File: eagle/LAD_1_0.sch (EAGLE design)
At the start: 14 parts, among them X1 A0, X10 A, X2 A1, X3 A2, X4 A3, X5 A, X6 A0, X7 A1, X8 A2, X9 A3

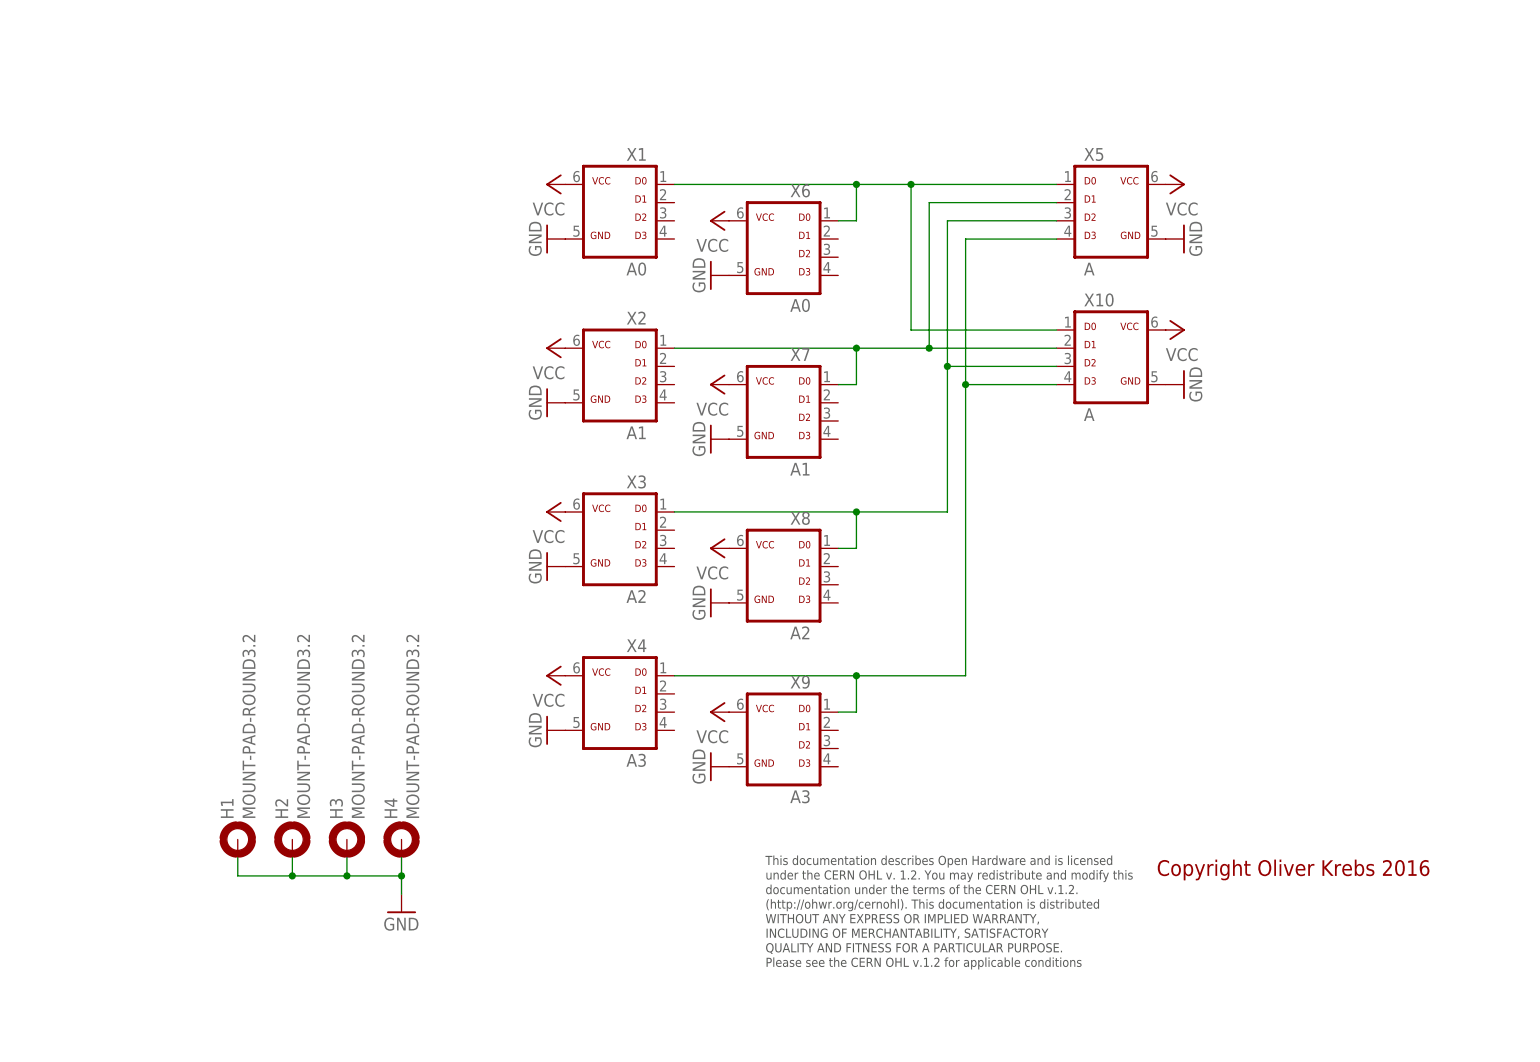
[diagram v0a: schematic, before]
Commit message: Add new tetra-Board and arduino files
Add AMP_1_0, AVC_1_0, D18_1_1, IOP_1_2, MIC_1_0, PIN_1_1, POT_1_0, PWA_1_0, PWR_1_0, RGF 2.0, SOC_2_0, VLT_1_0
Add mex_nano_shield_keyboard, mex_nano_shied_numbers

New arduino projects
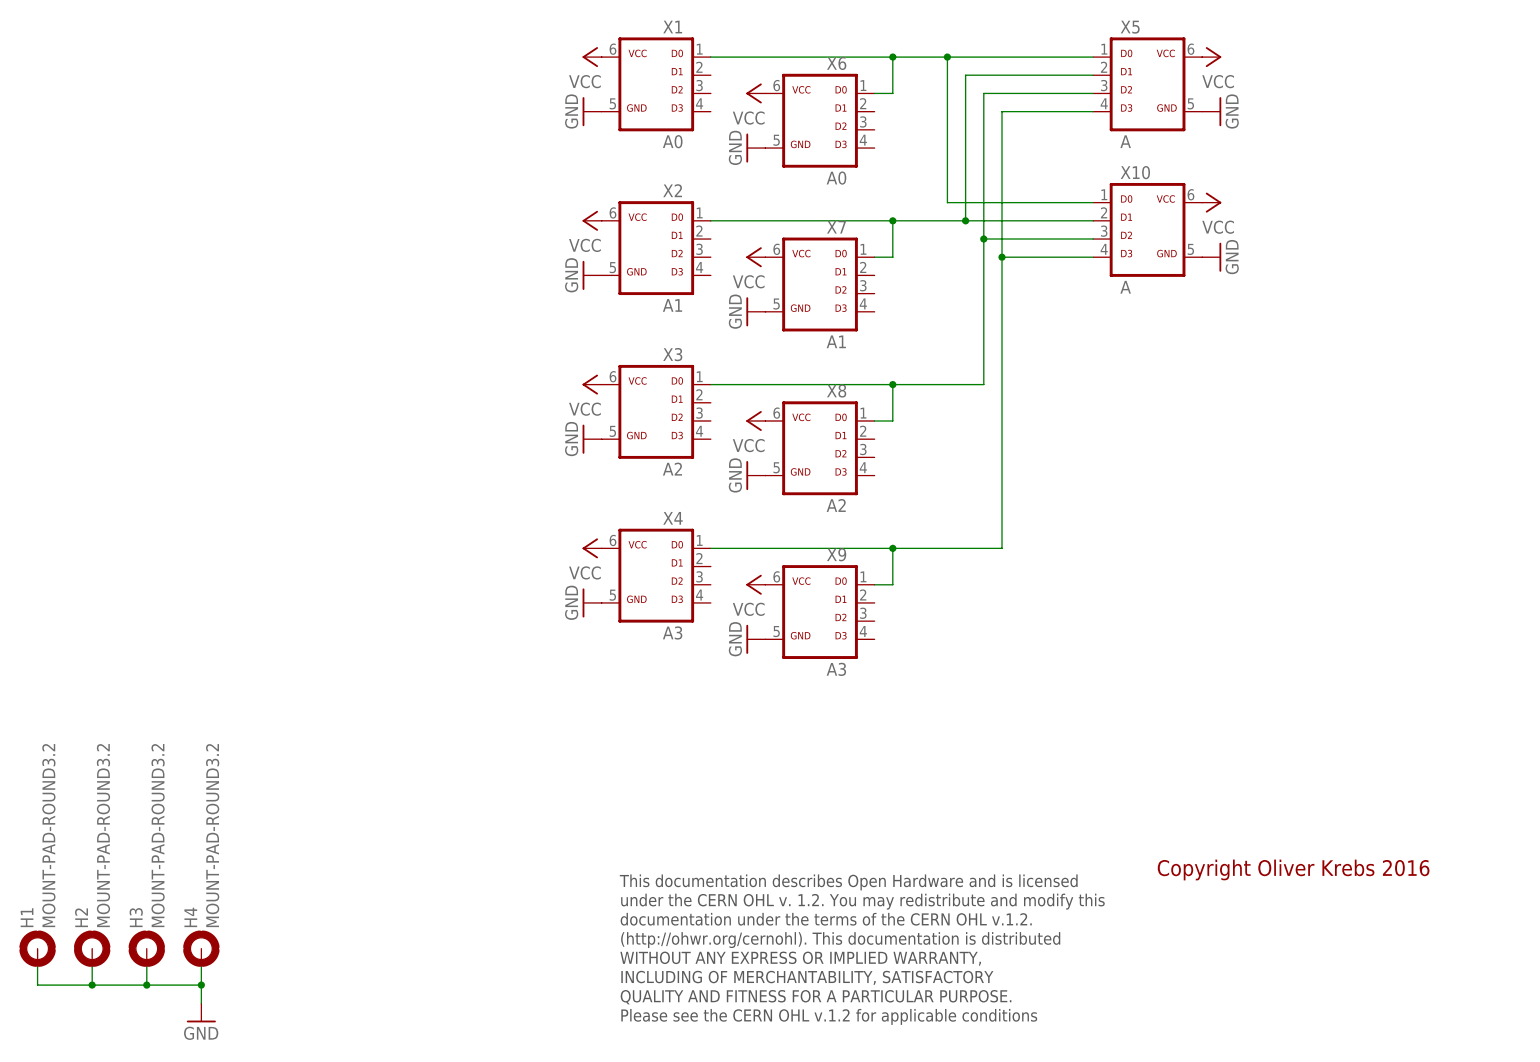
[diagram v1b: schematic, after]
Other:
- moved on the sheet: H1, H2, H3, H4, X1, X10, X2, X3, X4, X5, X6, X7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
